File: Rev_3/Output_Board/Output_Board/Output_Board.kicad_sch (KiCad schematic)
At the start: 26 parts, among them J1 6, J2 6, J3 6, J4 16, J5 6, K1 IM05GR, Q1 MMBT3904, Q2 DMP3099L, U1 TLP2361, U2 TLP170AM, U3 TLP170AM

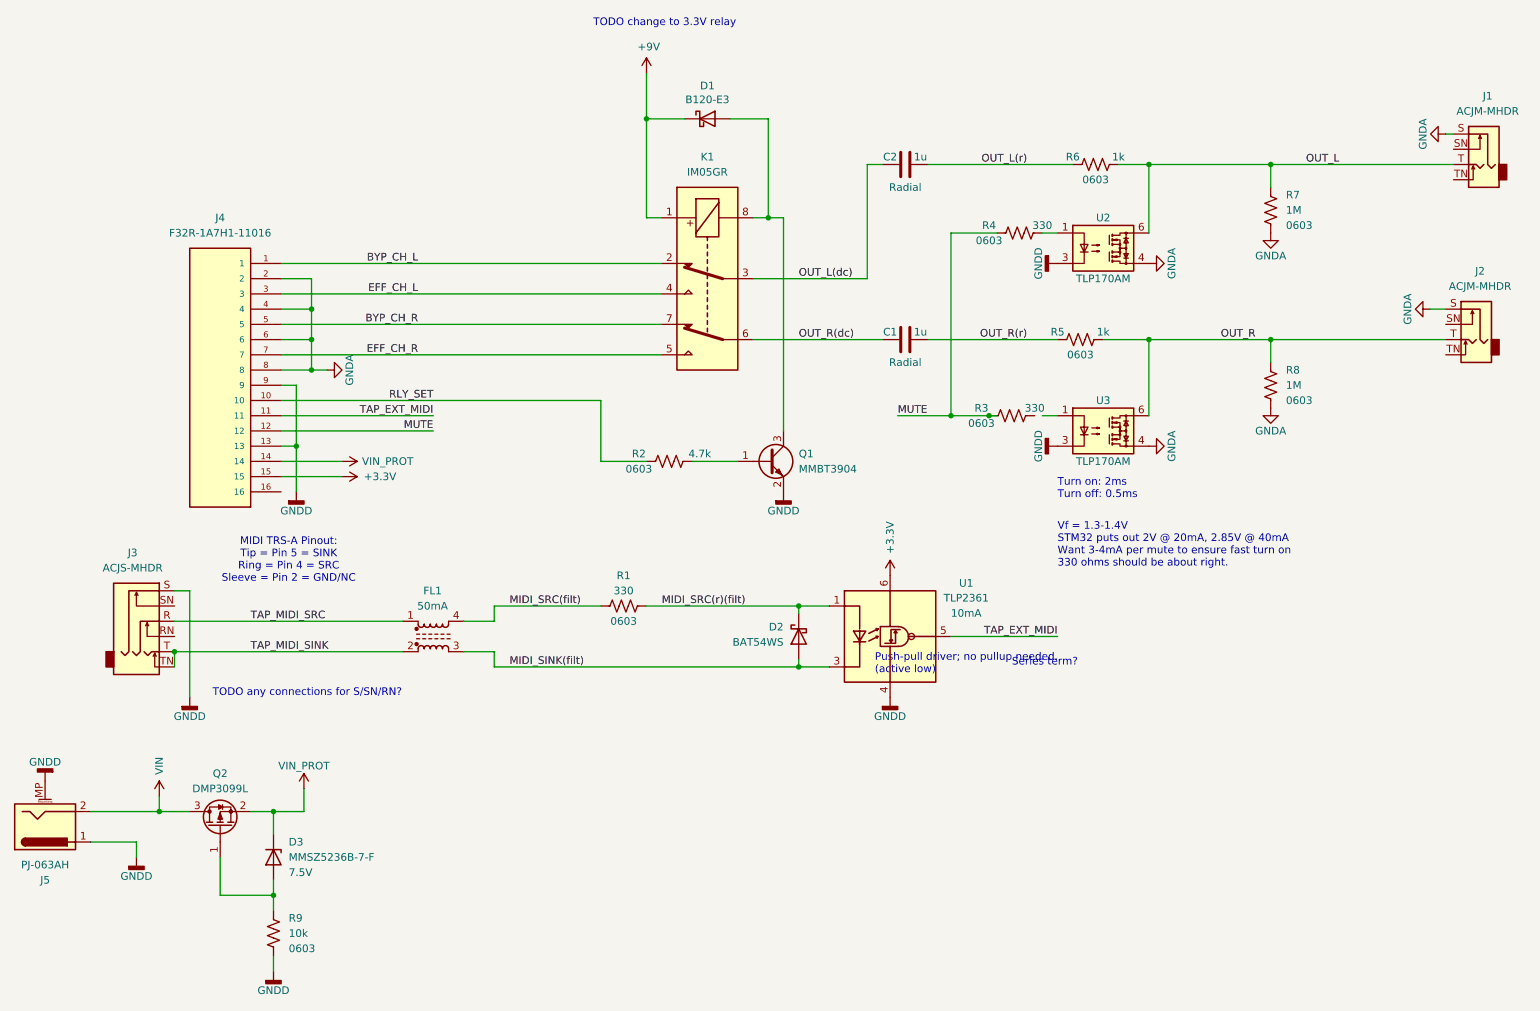
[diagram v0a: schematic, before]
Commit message: Added analog board back, switched to Jacks on Bottom
Added analog board mezzanine back to fit everything. Finalized decision on jack boards; jacks on bottom, wire to board connectors between jack boards and digital board. Tentative board outlines defined and scoped out component placement.
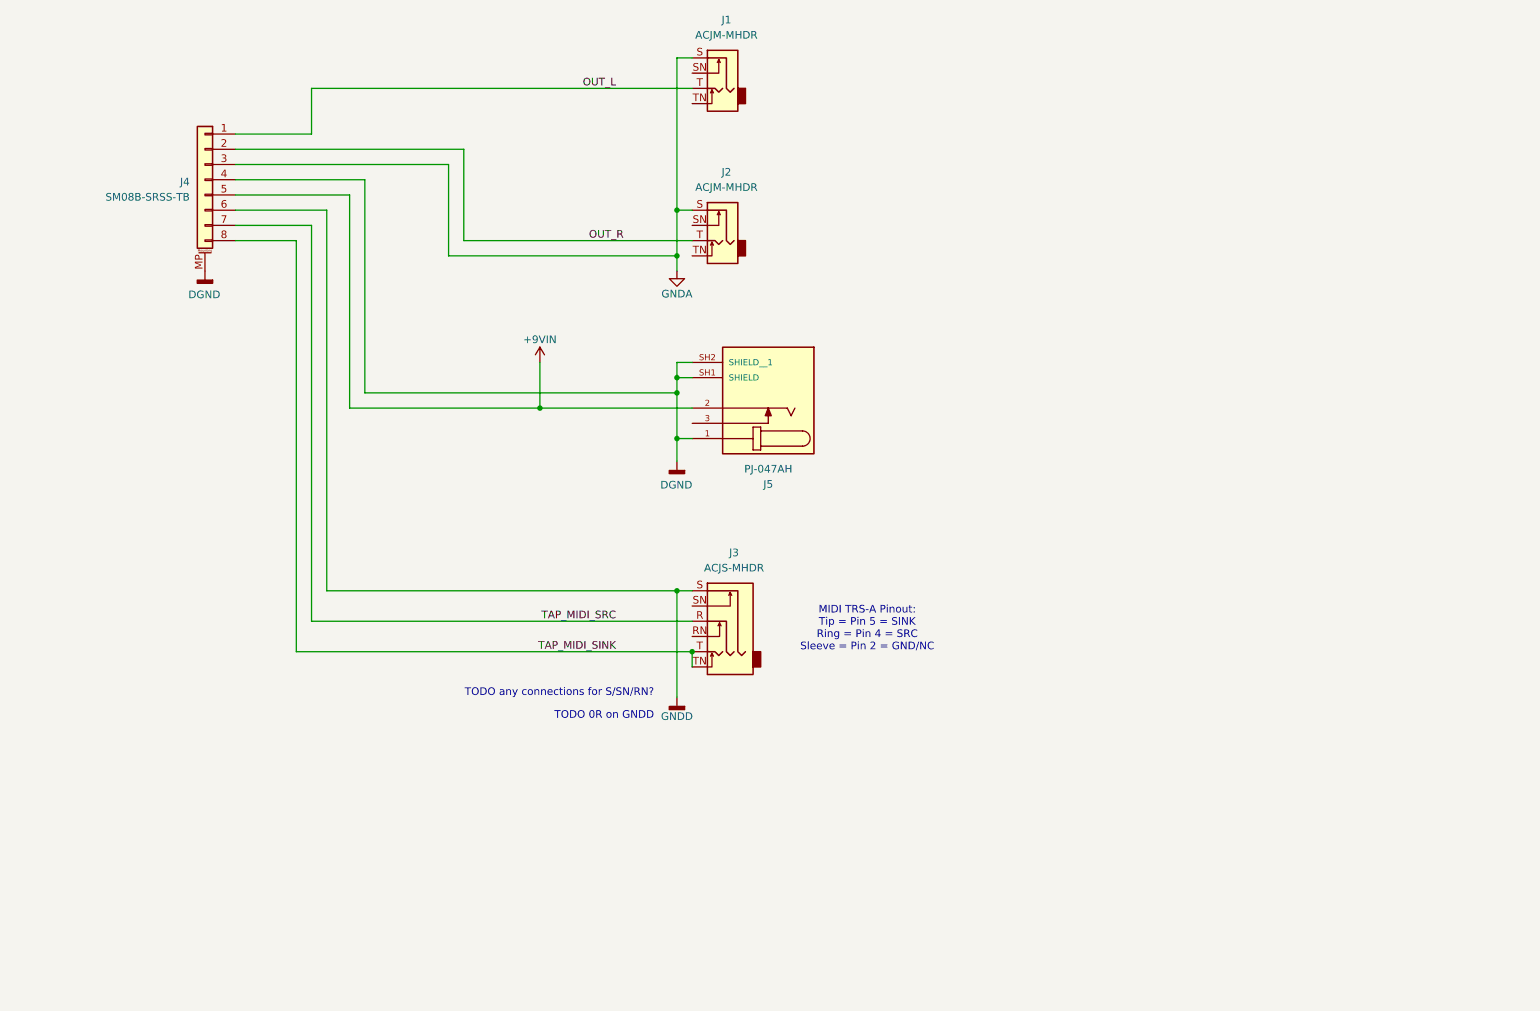
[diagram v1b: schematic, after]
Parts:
- removed C1, C2: 1u, Capacitor_THT:C_Rect_L7.2mm_W5.5mm_P5.00mm_FKS2_FKP2_MKS2_MKP2, symbol #gplm:cap/CAP-1003-0006
- removed D1: B120-E3, Diode_SMD:D_SMA, symbol Diode:B120-E3
- removed D2: BAT54WS, Diode_SMD:D_SOD-323, symbol #gplm:dio/DIO-0005-0001
- removed D3: MMSZ5236B-7-F, Diode_SMD:D_SOD-123, symbol #gplm:zen/ZEN-0002-07V5
- removed FL1: ~, g-ind:FIL_EXC-24CB102U, symbol #gplm:ind/IND-1001-0001
- removed J4: 16, g-con:AMPHENOL_F32R-1A7H1-11016, symbol #gplm:con/CON-1000-0016
- removed J5: 6, Connector_BarrelJack:BarrelJack_CUI_PJ-063AH_Horizontal, symbol #gplm:con/CON-1004-0001
- removed K1: IM05GR, g-rly:Relay_DPDT_TE_IM05GR, symbol #gplm:rly/RLY-0000-0109
- removed Q1: MMBT3904, Package_TO_SOT_SMD:SOT-23-3, symbol #gplm:bjt/XTR-0005-0001
- removed Q2: DMP3099L, Package_TO_SOT_SMD:SOT-23, symbol #gplm:fet/XTR-1001-0001
- removed R1, R3, R4: 330, Resistor_SMD:R_0603_1608Metric, symbol #gplm:res/RES-2001-330R
- removed R2: 4.7k, Resistor_SMD:R_0603_1608Metric, symbol #gplm:res/RES-2001-04K7
- removed R5, R6: 1k, Resistor_SMD:R_0603_1608Metric, symbol #gplm:res/RES-2001-001K
- removed R7, R8: 1M, Resistor_SMD:R_0603_1608Metric, symbol #gplm:res/RES-2001-001M
- removed R9: 10k, Resistor_SMD:R_0603_1608Metric, symbol #gplm:res/RES-2001-010K
- removed U1: TLP2361, Package_SO:SO-5-6_4.55x3.7mm_P1.27mm, symbol #gplm:opt/OPT-0003-0001
- removed U2, U3: TLP170AM, Package_SO:SO-4_4.4x3.9mm_P2.54mm, symbol #gplm:opt/OPT-0004-0001
- added J4: 8, Connector_JST:JST_SH_BM08B-SRSS-TB_1x08-1MP_P1.00mm_Vertical, symbol #gplm:con/CON-5001-0008
- added J5: 1, g-con:BarrelJack_CUI_PJ-047AH, symbol #gplm:con/CON-4001-0001
- J3: Manufacturer Neutrik -> Amphenol Audio; Pins 6 -> 4
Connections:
- net GNDA: now also J4.3 (Pin_3)
- net GNDD: now also J4.6 (Pin_6)
- net OUT_L: now also J4.1 (Pin_1)
- net OUT_R: now also J4.2 (Pin_2)
- net TAP_MIDI_SINK: now also J4.8 (Pin_8)
- net TAP_MIDI_SRC: now also J4.7 (Pin_7)
- new net +9VIN: J4.5 (Pin_5), J5.2
- new net DGND: J4.4 (Pin_4), J4.MP (MountPin), J5.1, J5.SH1 (SHIELD), J5.SH2 (SHIELD__1)
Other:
- note added: "TODO 0R on GNDD"
- note removed: "Push-pull driver; no pullup needed. (active low)"
- note removed: "Series term?"
- note removed: "TODO change to 3.3V relay"
- note removed: "Turn on: 2ms Turn off: 0.5ms"
- note removed: "Vf = 1.3-1.4V STM32 puts out 2V @ 20mA, 2.85V @ 40mA Want 3-4mA per mute to ensure fast turn on 330 ohms should be about right."
- moved on the sheet: J1, J2, J3

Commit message: Backing up before windows crash debug
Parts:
- removed J4: 8, Connector_JST:JST_SH_BM08B-SRSS-TB_1x08-1MP_P1.00mm_Vertical, symbol #gplm:con/CON-5001-0008
- added J6: 10, Connector_JST:JST_SH_BM10B-SRSS-TB_1x10-1MP_P1.00mm_Vertical, symbol #gplm:con/CON-5001-0010
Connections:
- net +9VIN: now also J6.5 (Pin_5)
- net DGND: no longer J5.1, J5.SH1 (SHIELD), J5.SH2 (SHIELD__1)
- net GNDA: now also J6.3 (Pin_3)
- net GNDD: now also J5.1, J5.SH1 (SHIELD), J5.SH2 (SHIELD__1), J6.4 (Pin_4), J6.6 (Pin_6)
- net OUT_L: now also J6.1 (Pin_1)
- net OUT_R: now also J6.2 (Pin_2)
- net TAP_MIDI_SINK: now also J6.8 (Pin_8)
- net TAP_MIDI_SRC: now also J6.7 (Pin_7)
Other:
- moved on the sheet: J3
